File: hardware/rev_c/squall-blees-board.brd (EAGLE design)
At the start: 25.4 x 21 mm, 19 parts, among them J1 SQUALL_HEADER, J4 HIROSE-DF40C-10DP-0.4V, J5 HIROSE-DF40C-10DP-0.4V

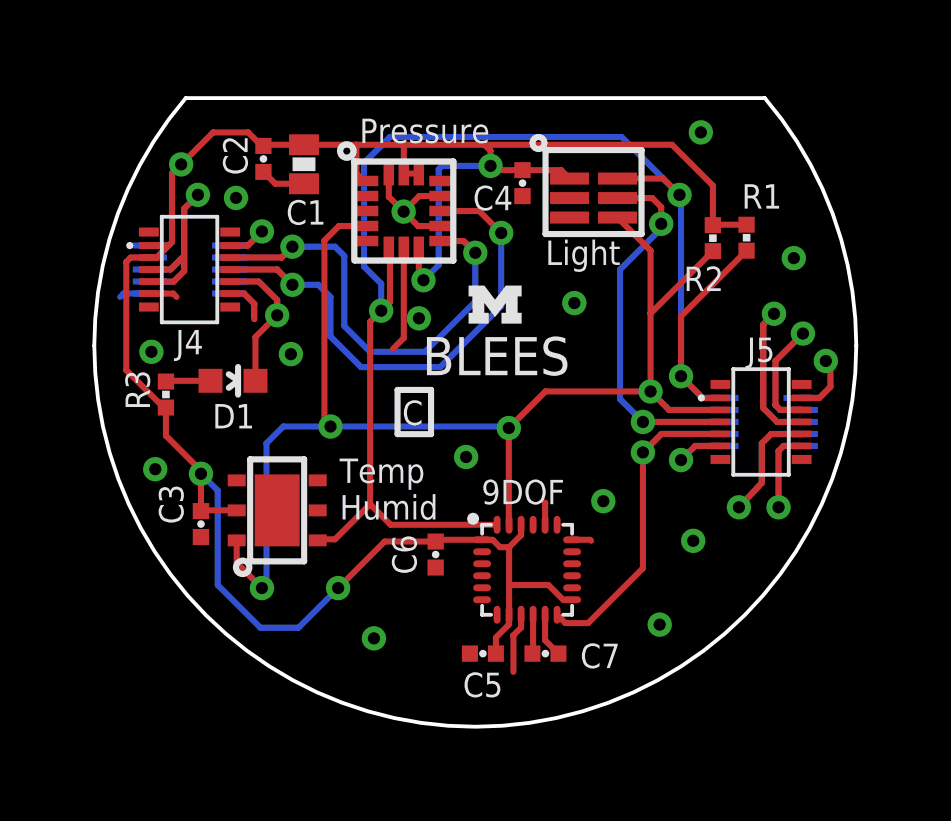
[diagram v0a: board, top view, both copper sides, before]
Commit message: Second pass at Rev C of BLEES. Added accelerometer
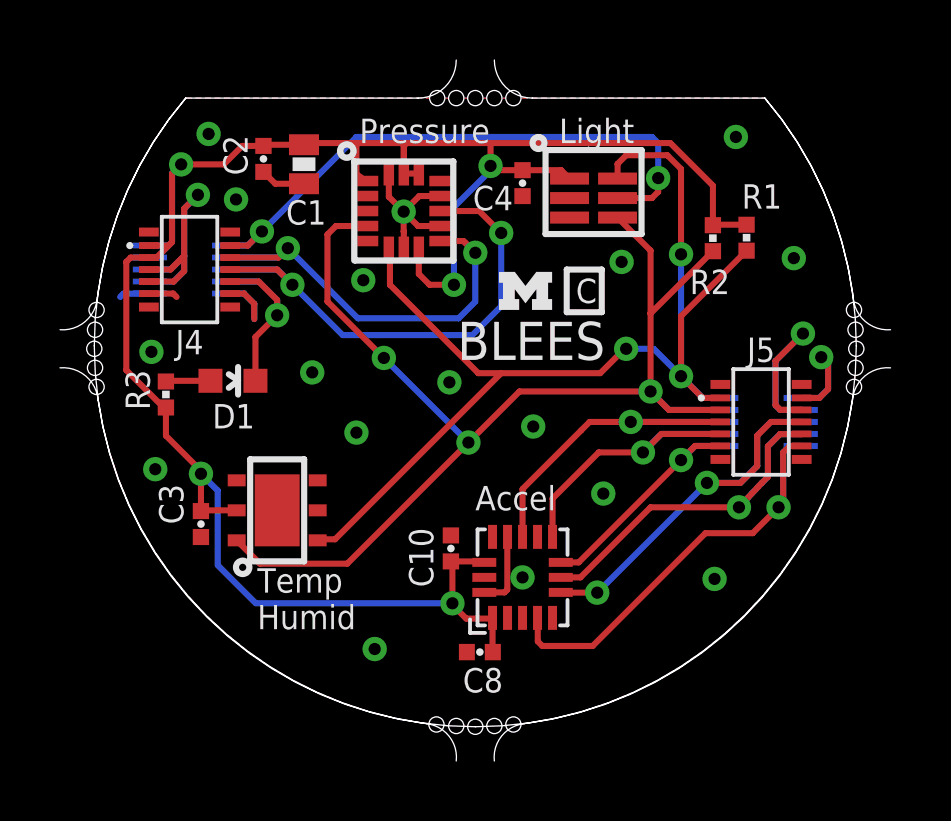
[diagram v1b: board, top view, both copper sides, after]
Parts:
- removed 9DOF: MPU-9250, chips:QFN-24/3MM
- removed C5, C7: 0.1uF, passives:0402_CAP
- removed C6: 10nF, passives:0402_CAP
- added C10, C8: 0.1uF, passives:0402_CAP
- added U1: ADXL362, SparkFun-Sensors:ADXL362
- moved U$1 1.11 mm to (25.8, 14.5)
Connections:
- removed net N$1: 9DOF.10, C7.1
- net A5: now also U1.P$8
- net A6: now also U1.P$9; no longer 9DOF.12
- net A7: now also U1.P$11; no longer LIGHT.5
- net GND: now also C10.2, C8.2, U1.P$12, U1.P$13, U1.P$16; no longer 9DOF.11, 9DOF.18, 9DOF.20, 9DOF.9, C5.2, C6.2, C7.2
- net MISO: now also U1.P$7
- net MOSI: now also U1.P$6
- net P22: now also LIGHT.5
- net SCL: no longer 9DOF.23
- net SCLK: now also U1.P$4
- net SDA: no longer 9DOF.24
- net VCC: now also C10.1, C8.1, U1.P$1, U1.P$14; no longer 9DOF.1, 9DOF.13, 9DOF.22, 9DOF.8, C5.1, C6.1
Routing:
- net P22: track 2.54 -> 20.2 mm, vias 1 -> 2
- net SCLK: track 5.40 -> 16.0 mm
- net SDA: track 49.3 -> 39.6 mm
- net MISO: track 7.75 -> 14.3 mm
- net MOSI: track 9.50 -> 15.5 mm, vias 1 -> 2
- net A5: track 3.05 -> 8.47 mm
- net VCC: track 77.2 -> 72.3 mm
- net GND: track 19.6 -> 14.9 mm, vias 14 -> 17
- net SCL: track 46.2 -> 41.5 mm, vias 4 -> 3
- net A7: track 14.8 -> 12.1 mm, vias 2 -> 1
- net A6: track 13.3 -> 10.6 mm
- net P23: track 17.5 -> 15.0 mm
- net P24: track 19.1 -> 17.4 mm
- net N$1: track 1.30 -> 0.00 mm
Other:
- board size 25.4 x 21 mm -> 27.7 x 23.4 mm
- board text added: "Accel"
- board text removed: "9DOF"

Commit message: Panelized version of rev C BLEES
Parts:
- removed C10: 0.1uF, passives:0402_CAP
- removed PRESSURE: LPS331APQFN, blees:HCLGA-16L
- added C6: 10uF, passives:0603_CAP
- added U4: ADXL362, SparkFun-Sensors:ADXL362
- C1: value 10uF -> 100nF; device passives:0603_CAP -> passives:0402_CAP
- C4: value 100nF -> 0.1uF
- R1: value 2kΩ -> 1kΩ
- R3: value 1kΩ -> 2kΩ
- U1: value ADXL362 -> LPS331APQFN; device SparkFun-Sensors:ADXL362 -> blees:HCLGA-16L
- moved R1 20.0 mm to (13.8, 11.1), turned to 270 degrees
- moved R3 20.0 mm to (33.2, 16.3), turned to 90 degrees
- moved U1 12.8 mm to (21.7, 17.2), turned to 0 degrees
- moved C4 12.4 mm to (23.3, 5.94), turned to 90 degrees
- moved C2 8.67 mm to (25.7, 18.1)
- moved C1 1.36 mm to (17.1, 18.9)
- renumbered C8 to C5, J4 to J2, J5 to J3, LIGHT to U2, TEMP/HUMID to U3
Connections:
- net A5: now also U4.P$8; no longer U1.P$8
- net A6: now also U4.P$9; no longer U1.P$9
- net A7: now also U4.P$11; no longer U1.P$11
- net GND: now also C6.2, U1.10, U1.12, U1.13, U1.16, U1.5, U1.7, U4.P$12, U4.P$13, U4.P$16; no longer C10.2, PRESSURE.10, PRESSURE.12, PRESSURE.13, PRESSURE.16, PRESSURE.5, PRESSURE.7, U1.P$12, U1.P$13, U1.P$16
- net MISO: now also U4.P$7; no longer U1.P$7
- net MOSI: now also U4.P$6; no longer U1.P$6
- net N$2: now also R1.1; no longer R3.1
- net P23: now also U1.9; no longer PRESSURE.9
- net P24: now also U1.11; no longer PRESSURE.11
- net SCL: now also U1.4; no longer PRESSURE.4
- net SCLK: now also U4.P$4; no longer U1.P$4
- net SDA: now also R3.1, U1.6; no longer PRESSURE.6, R1.1
- net VCC: now also C6.1, U1.1, U1.14, U1.15, U1.8, U4.P$1, U4.P$14; no longer C10.1, PRESSURE.1, PRESSURE.14, PRESSURE.15, PRESSURE.8, U1.P$1, U1.P$14

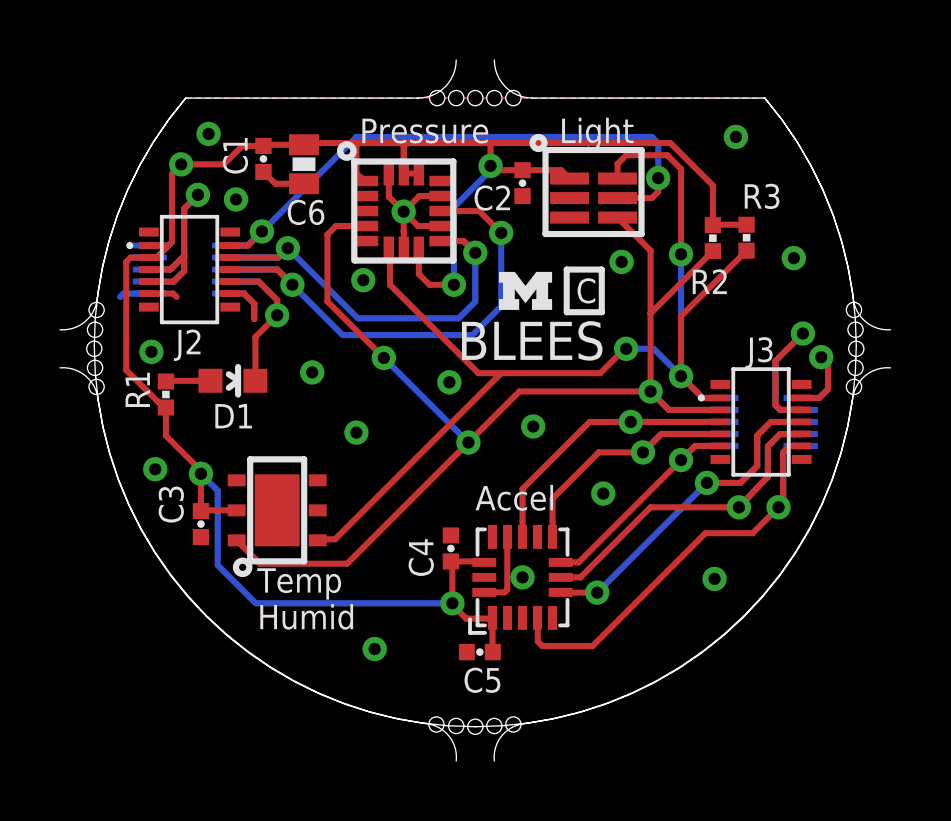
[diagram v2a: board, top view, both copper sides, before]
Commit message: Swapped out temp/humidity sensor
This one is lower power, same functionality, and purchasable
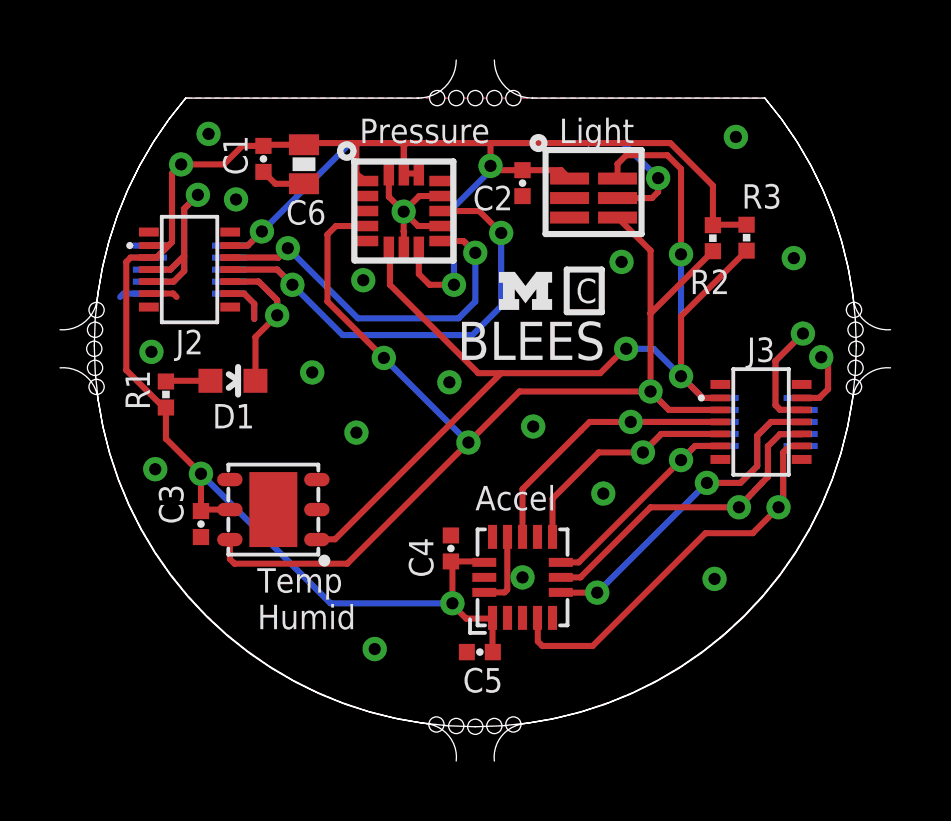
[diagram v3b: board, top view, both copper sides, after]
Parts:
- C4, C5: value 0.1uF -> 100nF
- R2, R3: value 2kΩ -> 10k
- U3: value HTU21DDFN -> SI7021; device blees:DFN -> chips:DFN-6/3MM
- moved U3 0.13 mm to (17.4, 7.24), turned to 180 degrees
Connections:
- net GND: now also U3.2; no longer U3.5, U3.PAD
- net SCL: now also U3.6; no longer U3.1
- net SDA: now also U3.1; no longer U3.6
- net VCC: now also U3.5; no longer U3.2
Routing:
- net VCC: track 72.3 -> 70.7 mm
- net P22: track 20.2 -> 19.4 mm
- net SCL: track 41.5 -> 42.1 mm
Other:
- board text added: "2015/06/12"
- board text added: "J1"
- board text removed: "2015/06/09"
